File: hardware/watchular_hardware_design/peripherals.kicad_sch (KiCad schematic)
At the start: 47 parts, among them J3 TSW-115-07-H-S, J4 TSW-115-07-H-S, Q1 BSS123, Q2 BSS123, Q3 BSS123, Q4 BSS123

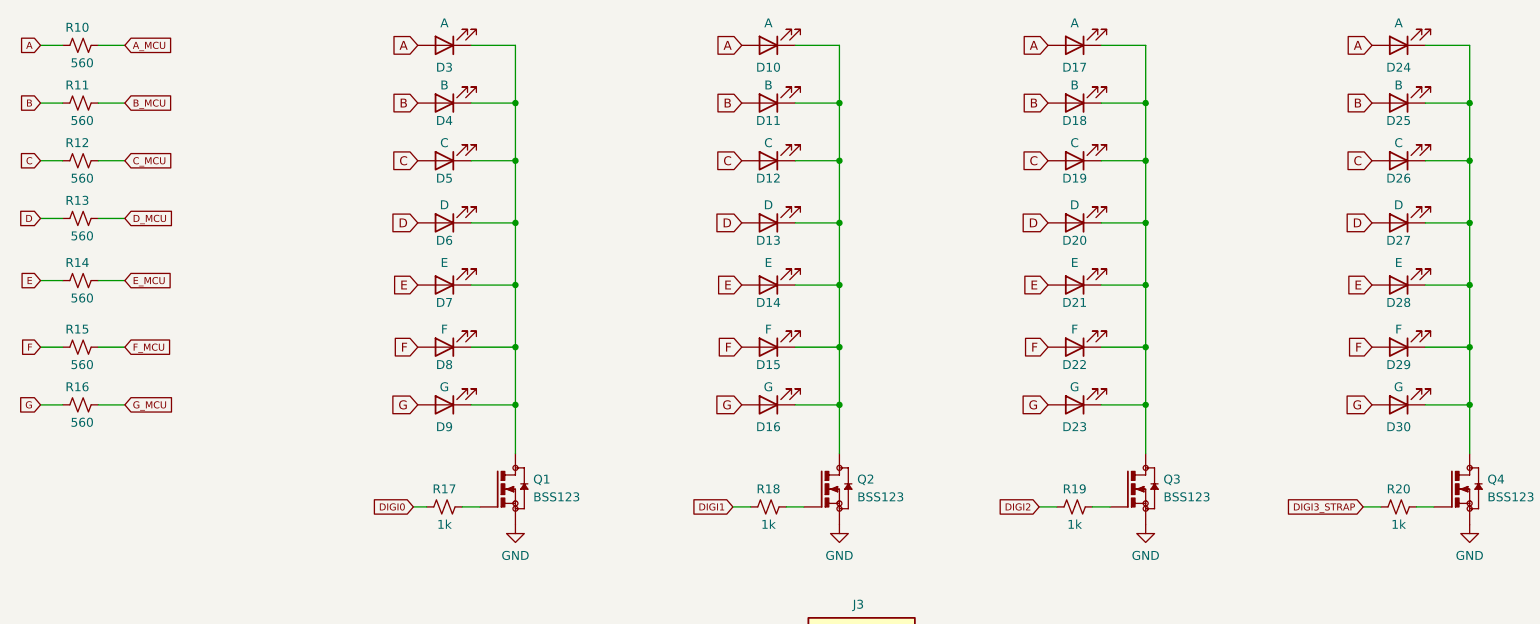
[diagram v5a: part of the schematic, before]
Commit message: Dual power wired up
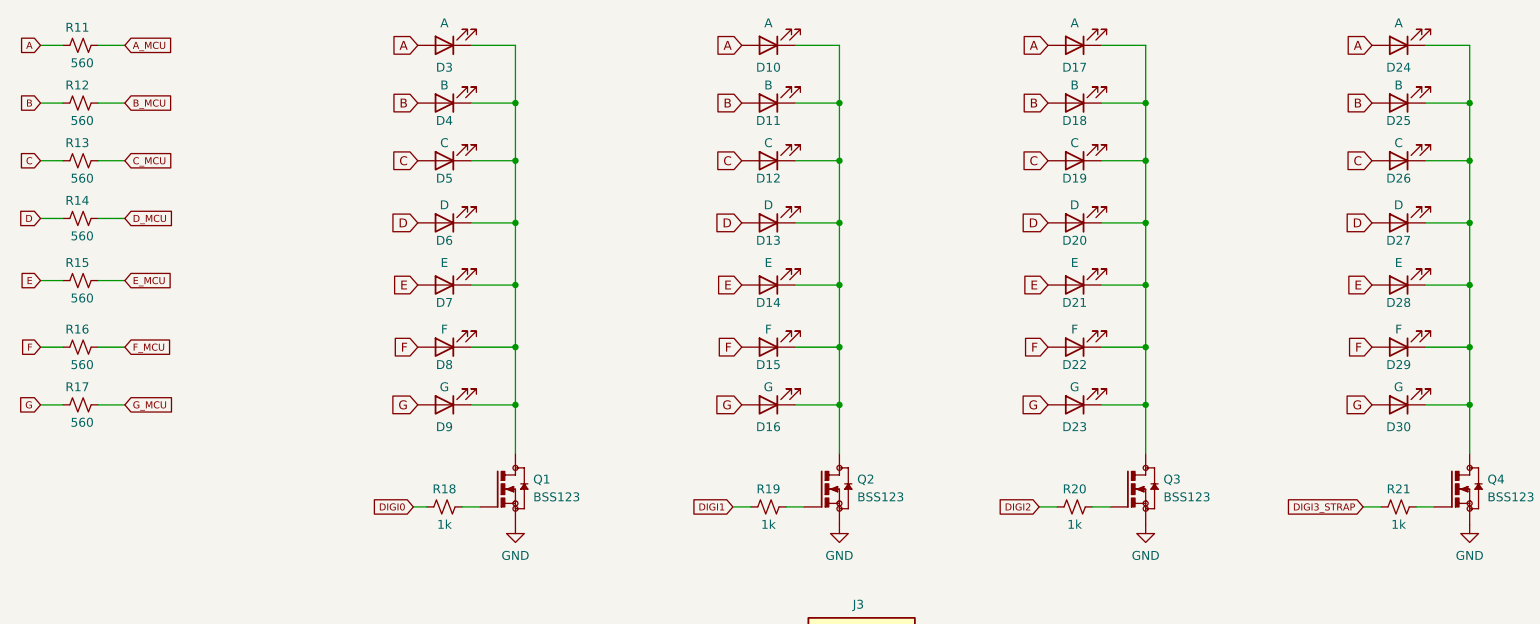
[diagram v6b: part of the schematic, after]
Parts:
- renumbered R10 to R11, R11 to R12, R12 to R13, R13 to R14, R14 to R15, R15 to R16, R16 to R17, R17 to R18, R18 to R19, R19 to R20, R20 to R21
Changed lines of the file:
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@@
   (symbol (lib_id "Device:R_Small_US") (at 80.01 85.725 90) (unit 1)
     (in_bom yes) (on_board yes)
-    (property "Reference" "R17" (id 0) (at 80.01 83.185 90))
+    (property "Reference" "R18" (id 0) (at 80.01 83.185 90))
     (property "Value" "1k" (id 1) (at 80.01 88.265 90))
     (property "Footprint" "Resistor_SMD:R_0402_1005Metric_Pad0.72x0.64mm_HandSolder" (id 2) (at 80.01 85.725 0)
@@
   (symbol (lib_id "Device:R_Small_US") (at 170.18 85.725 90) (unit 1)
     (in_bom yes) (on_board yes)
-    (property "Reference" "R19" (id 0) (at 170.18 83.185 90))
+    (property "Reference" "R20" (id 0) (at 170.18 83.185 90))
     (property "Value" "1k" (id 1) (at 170.18 88.265 90))
     (property "Footprint" "Resistor_SMD:R_0402_1005Metric_Pad0.72x0.64mm_HandSolder" (id 2) (at 170.18 85.725 0)
@@
   (symbol (lib_id "power:GND") (at 38.735 122.555 0) (unit 1)
     (in_bom yes) (on_board yes) (fields_autoplaced)
-    (property "Reference" "#PWR037" (id 0) (at 38.735 128.905 0)
+    (property "Reference" "#PWR041" (id 0) (at 38.735 128.905 0)
       (effects (font (size 1.27 1.27)) hide)
     )
@@
   (symbol (lib_id "power:GND") (at 90.17 88.265 0) (unit 1)
     (in_bom yes) (on_board yes) (fields_autoplaced)
-    (property "Reference" "#PWR039" (id 0) (at 90.17 94.615 0)
+    (property "Reference" "#PWR043" (id 0) (at 90.17 94.615 0)
       (effects (font (size 1.27 1.27)) hide)
     )
@@
   (symbol (lib_id "power:GND") (at 136.525 88.265 0) (unit 1)
     (in_bom yes) (on_board yes) (fields_autoplaced)
-    (property "Reference" "#PWR041" (id 0) (at 136.525 94.615 0)
+    (property "Reference" "#PWR045" (id 0) (at 136.525 94.615 0)
       (effects (font (size 1.27 1.27)) hide)
     )
@@
   (symbol (lib_id "Device:R_Small_US") (at 27.94 71.12 90) (unit 1)
     (in_bom yes) (on_board yes)
-    (property "Reference" "R16" (id 0) (at 29.21 68.58 90)
+    (property "Reference" "R17" (id 0) (at 29.21 68.58 90)
       (effects (font (size 1.27 1.27)) (justify left))
     )
@@
   (symbol (lib_id "Device:R_Small_US") (at 216.535 85.725 90) (unit 1)
     (in_bom yes) (on_board yes)
-    (property "Reference" "R20" (id 0) (at 216.535 83.185 90))
+    (property "Reference" "R21" (id 0) (at 216.535 83.185 90))
     (property "Value" "1k" (id 1) (at 216.535 88.265 90))
     (property "Footprint" "Resistor_SMD:R_0402_1005Metric_Pad0.72x0.64mm_HandSolder" (id 2) (at 216.535 85.725 0)
@@
   (symbol (lib_id "Device:R_Small_US") (at 126.365 85.725 90) (unit 1)
     (in_bom yes) (on_board yes)
-    (property "Reference" "R18" (id 0) (at 126.365 83.185 90))
+    (property "Reference" "R19" (id 0) (at 126.365 83.185 90))
     (property "Value" "1k" (id 1) (at 126.365 88.265 90))
     (property "Footprint" "Resistor_SMD:R_0402_1005Metric_Pad0.72x0.64mm_HandSolder" (id 2) (at 126.365 85.725 0)
@@
   (symbol (lib_id "power:GND") (at 39.37 140.97 0) (unit 1)
     (in_bom yes) (on_board yes) (fields_autoplaced)
-    (property "Reference" "#PWR038" (id 0) (at 39.37 147.32 0)
+    (property "Reference" "#PWR042" (id 0) (at 39.37 147.32 0)
       (effects (font (size 1.27 1.27)) hide)
     )
@@
   (symbol (lib_id "Device:R_Small_US") (at 27.94 36.195 90) (unit 1)
     (in_bom yes) (on_board yes)
-    (property "Reference" "R12" (id 0) (at 29.21 33.655 90)
+    (property "Reference" "R13" (id 0) (at 29.21 33.655 90)
       (effects (font (size 1.27 1.27)) (justify left))
     )
@@
   (symbol (lib_id "Device:R_Small_US") (at 27.94 27.94 90) (unit 1)
     (in_bom yes) (on_board yes)
-    (property "Reference" "R11" (id 0) (at 29.21 25.4 90)
+    (property "Reference" "R12" (id 0) (at 29.21 25.4 90)
       (effects (font (size 1.27 1.27)) (justify left))
     )
@@
   (symbol (lib_id "Device:R_Small_US") (at 27.94 44.45 90) (unit 1)
     (in_bom yes) (on_board yes)
-    (property "Reference" "R13" (id 0) (at 29.21 41.91 90)
+    (property "Reference" "R14" (id 0) (at 29.21 41.91 90)
       (effects (font (size 1.27 1.27)) (justify left))
     )
@@
   (symbol (lib_id "power:GND") (at 180.34 88.265 0) (unit 1)
     (in_bom yes) (on_board yes) (fields_autoplaced)
-    (property "Reference" "#PWR042" (id 0) (at 180.34 94.615 0)
+    (property "Reference" "#PWR046" (id 0) (at 180.34 94.615 0)
       (effects (font (size 1.27 1.27)) hide)
     )
@@
   (symbol (lib_id "Device:R_Small_US") (at 27.94 19.685 90) (unit 1)
     (in_bom yes) (on_board yes)
-    (property "Reference" "R10" (id 0) (at 29.21 17.145 90)
+    (property "Reference" "R11" (id 0) (at 29.21 17.145 90)
       (effects (font (size 1.27 1.27)) (justify left))
     )
@@
   (symbol (lib_id "power:GND") (at 113.665 104.14 0) (unit 1)
     (in_bom yes) (on_board yes)
-    (property "Reference" "#PWR040" (id 0) (at 113.665 110.49 0)
+    (property "Reference" "#PWR044" (id 0) (at 113.665 110.49 0)
       (effects (font (size 1.27 1.27)) hide)
     )
@@
   (symbol (lib_id "Device:R_Small_US") (at 27.94 53.34 90) (unit 1)
     (in_bom yes) (on_board yes)
-    (property "Reference" "R14" (id 0) (at 29.21 50.8 90)
+    (property "Reference" "R15" (id 0) (at 29.21 50.8 90)
       (effects (font (size 1.27 1.27)) (justify left))
     )
@@
   (symbol (lib_id "power:GND") (at 226.695 88.265 0) (unit 1)
     (in_bom yes) (on_board yes) (fields_autoplaced)
-    (property "Reference" "#PWR043" (id 0) (at 226.695 94.615 0)
+    (property "Reference" "#PWR047" (id 0) (at 226.695 94.615 0)
       (effects (font (size 1.27 1.27)) hide)
     )
@@
   (symbol (lib_id "Device:R_Small_US") (at 27.94 62.865 90) (unit 1)
     (in_bom yes) (on_board yes)
-    (property "Reference" "R15" (id 0) (at 29.21 60.325 90)
-      (effects (font (size 1.27 1.27)) (justify left))
-    )
+    (property "Reference" "R16" (id 0) (at 29.21 60.325 90)
+      (effects (font (size 1.27 1.27)) (justify left))
+    )

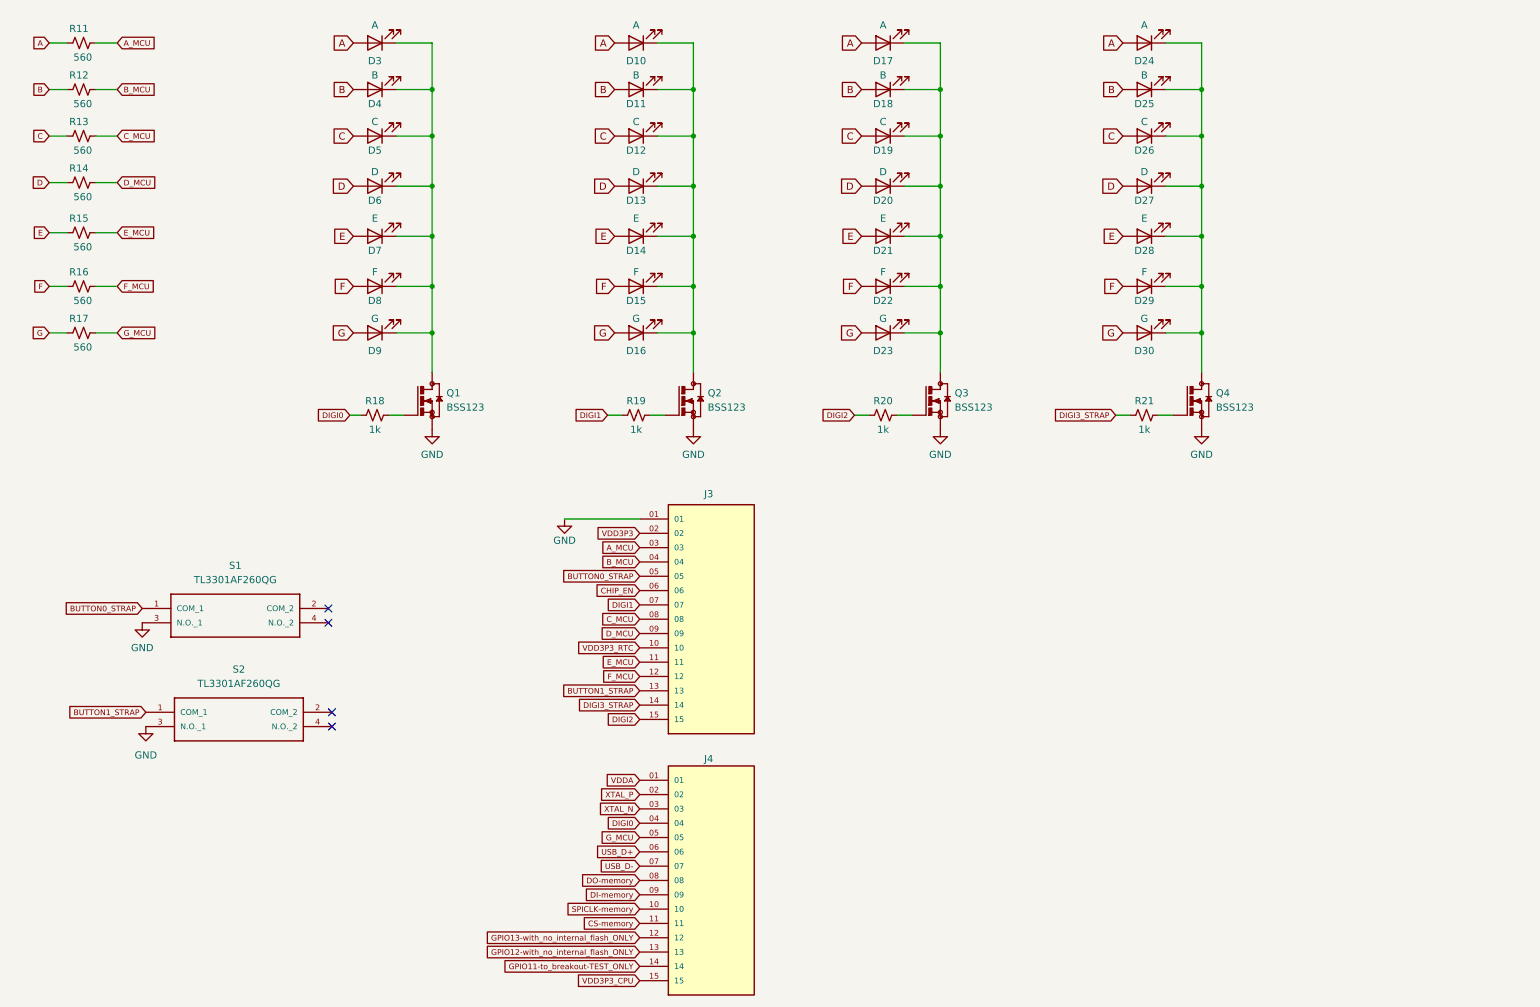
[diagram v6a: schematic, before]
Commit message: Added back the 16 pin headers.
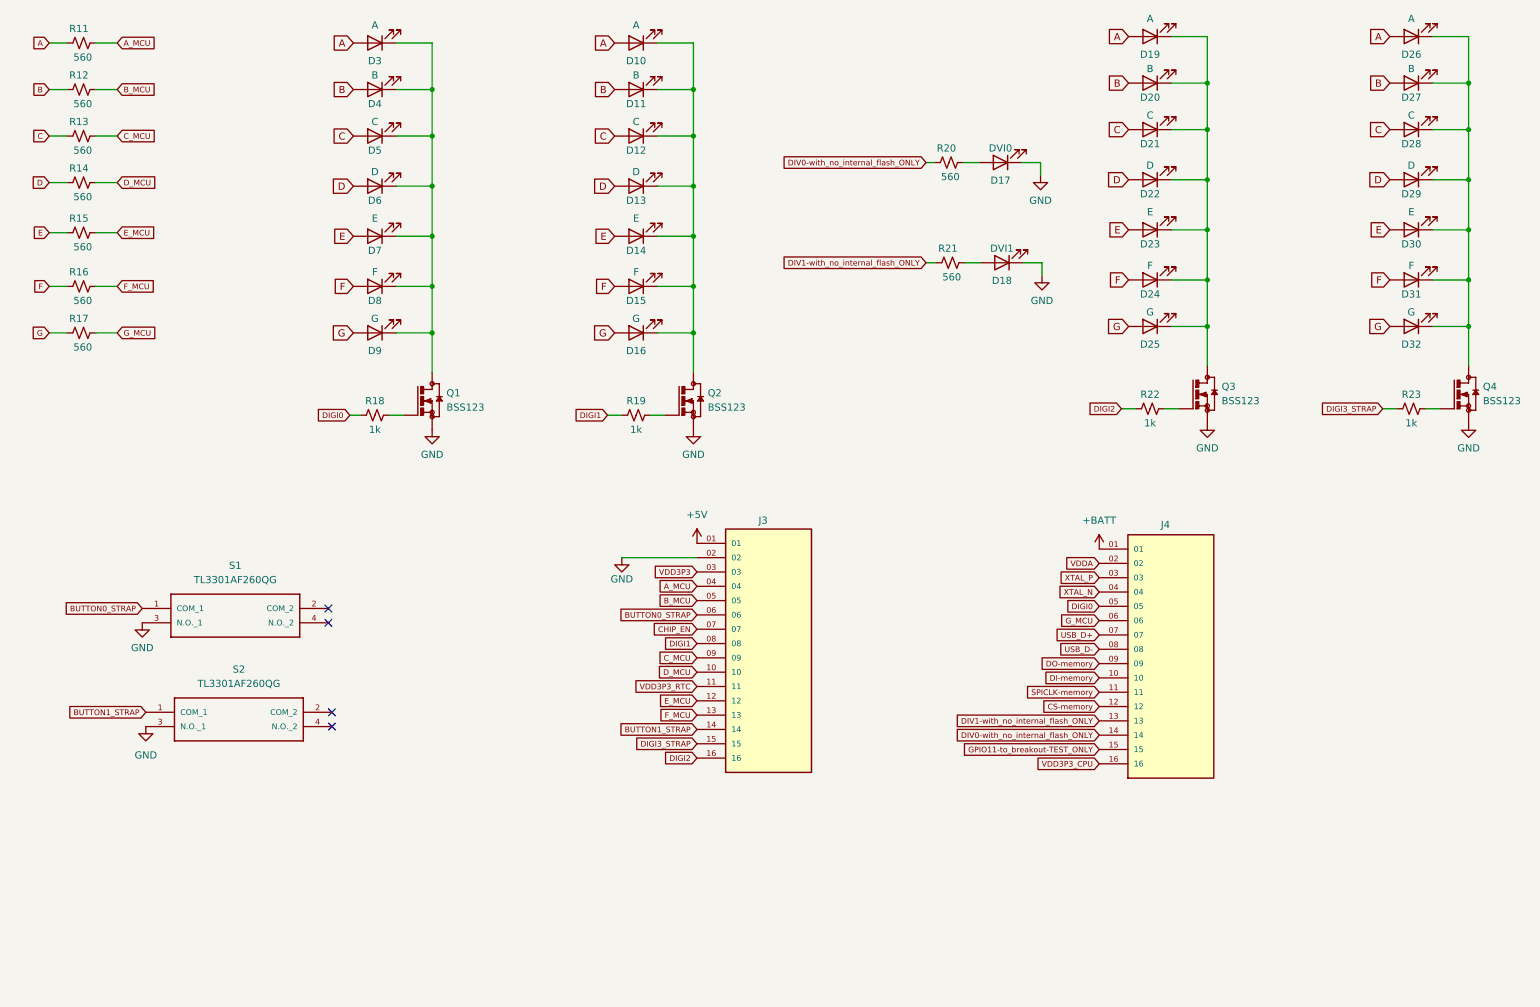
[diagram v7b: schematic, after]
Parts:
- removed J3, J4: TSW-115-07-H-S, header-TSW-115-07-H-S:SAMTEC_TSW-115-07-H-S, symbol TSW-115-07-H-S:TSW-115-07-H-S
- added D17: DVI0, LED_SMD:LED_0603_1608Metric, symbol Device:LED
- added D18: DVI1, LED_SMD:LED_0603_1608Metric, symbol Device:LED
- added J3, J4: TSW-116-07-H-S, SAMTEC_TSW-116-07-H-S, symbol TSW-116-07-H-S:TSW-116-07-H-S
- added R20, R21: 560, Resistor_SMD:R_0402_1005Metric_Pad0.72x0.64mm_HandSolder, symbol Device:R_Small_US
- renumbered D17 to D19, D18 to D20, D19 to D21, D20 to D22, D21 to D23, D22 to D24, D23 to D25, D24 to D26, D25 to D27, D26 to D28, D27 to D29, D28 to D30, D29 to D31, D30 to D32, R20 to R22, R21 to R23
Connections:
- net A_MCU: now also J3.04
- net BUTTON0_STRAP: now also J3.06
- net BUTTON1_STRAP: now also J3.14
- net B_MCU: now also J3.05
- net CHIP_EN: now also J3.07
- net CS-memory: now also J4.12
- net C_MCU: now also J3.09
- net DI-memory: now also J4.10
- net DIGI0: now also J4.05
- net DIGI1: now also J3.08
- net DIGI2: now also J3.16
- net DIGI3_STRAP: now also J3.15
- net DO-memory: now also J4.09
- net D_MCU: now also J3.10
- net E_MCU: now also J3.12
- net F_MCU: now also J3.13
- net GND: now also D17.1 (K), D18.1 (K), J3.02
- net GPIO11-to_breakout-TEST_ONLY: now also J4.15
- net G_MCU: now also J4.06
- net SPICLK-memory: now also J4.11
- net USB_D+: now also J4.07
- net USB_D-: now also J4.08
- net VDD3P3: now also J3.03
- net VDD3P3_CPU: now also J4.16
- net VDD3P3_RTC: now also J3.11
- net VDDA: now also J4.02
- net XTAL_N: now also J4.04
- net XTAL_P: now also J4.03
- new net: D18.2 (A), R21.2
- new net: D17.2 (A), R20.2
- new net +5V: J3.01
- new net +BATT: J4.01
- new net DIV0-with_no_internal_flash_ONLY: J4.14, R20.1
- new net DIV1-with_no_internal_flash_ONLY: J4.13, R21.1
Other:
- moved on the sheet: D19, D20, D21, D22, D23, D24, D25, D26, D27, D28, D29, D30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

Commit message: Schematic is done for now.
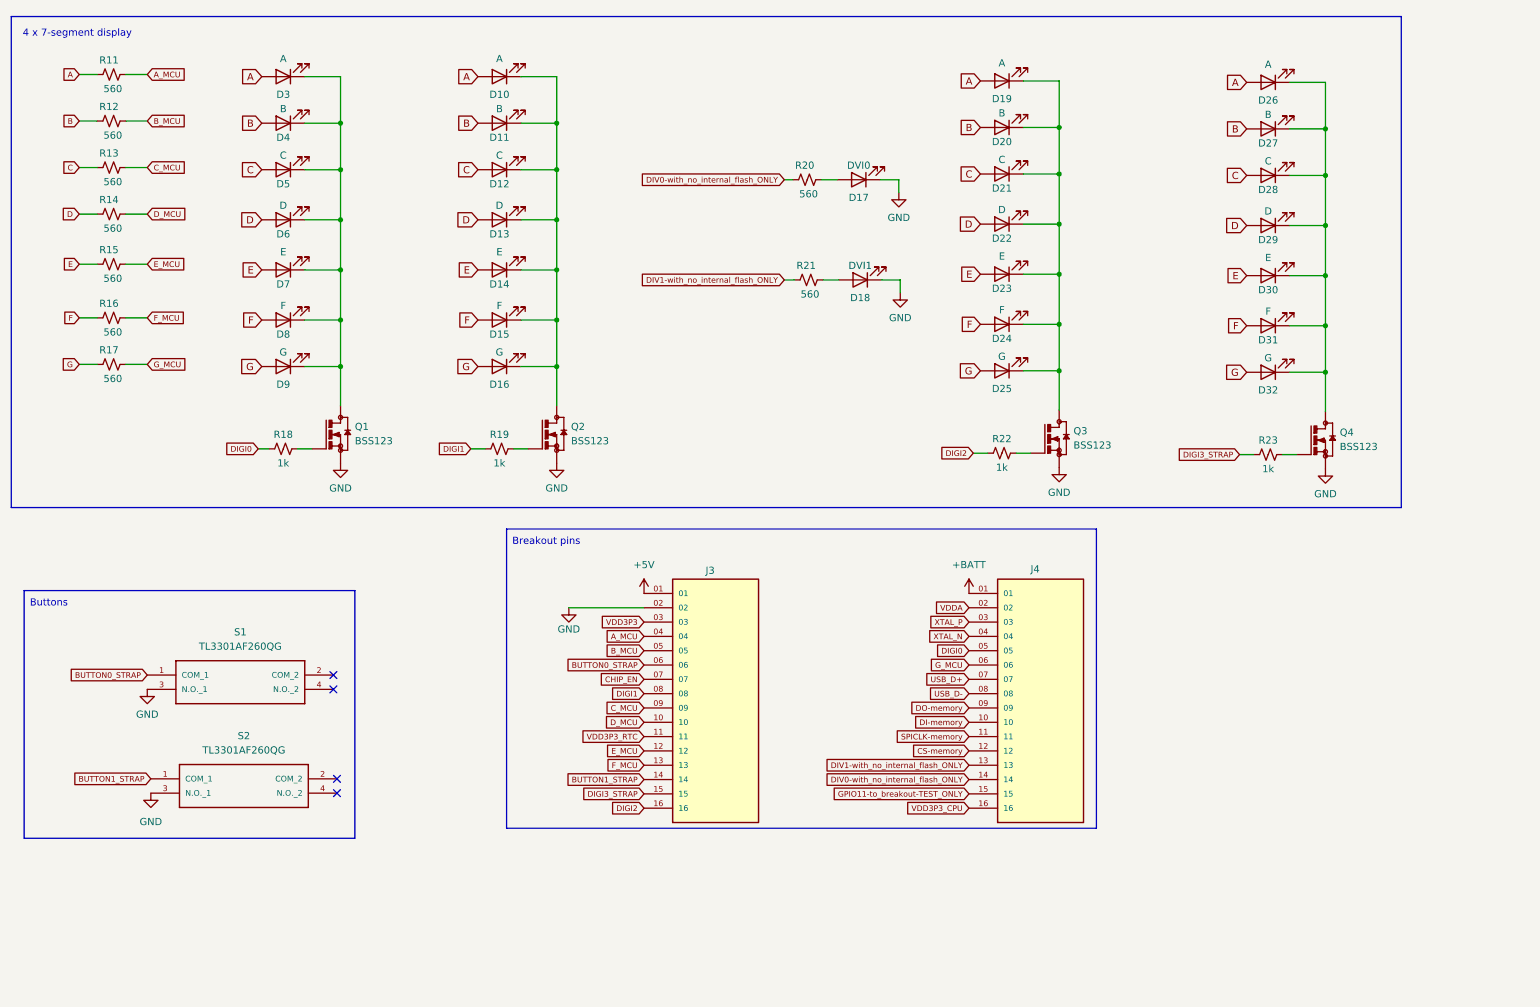
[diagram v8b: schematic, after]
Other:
- note added: "4 x 7-segment display"
- note added: "Breakout pins"
- note added: "Buttons"
- moved on the sheet: D10, D11, D12, D13, D14, D15, D16, D17, D18, D19, D20, D21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
